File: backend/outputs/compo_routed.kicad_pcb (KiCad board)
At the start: 4 copper layers, 56 x 55 mm, 20 parts, among them J1 Conn_01x06_Pin, J2 Barrel_Jack, J3 Conn_01x02_Pin, U2 MIC5504-1.2YM5, U3 ATmega164P-20P

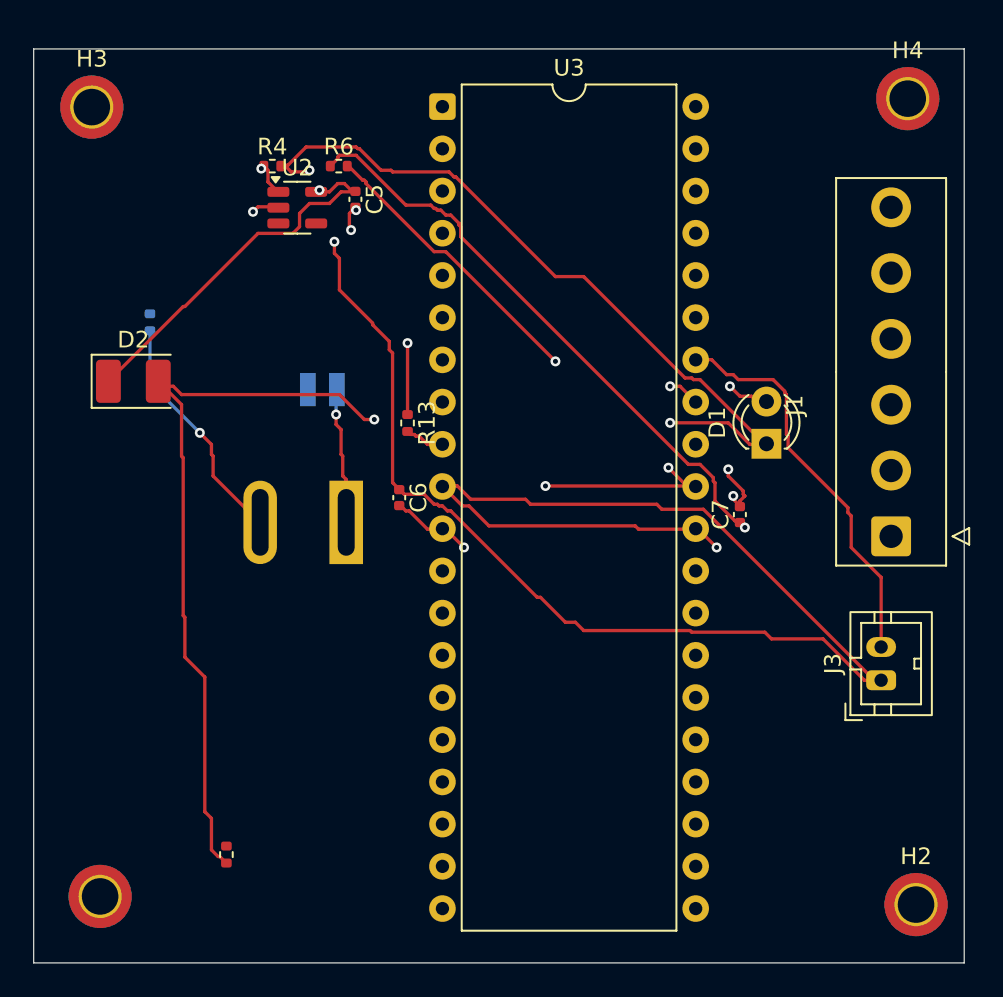
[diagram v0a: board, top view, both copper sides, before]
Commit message: Integrated Gemini 2.0 and added routing dashboard
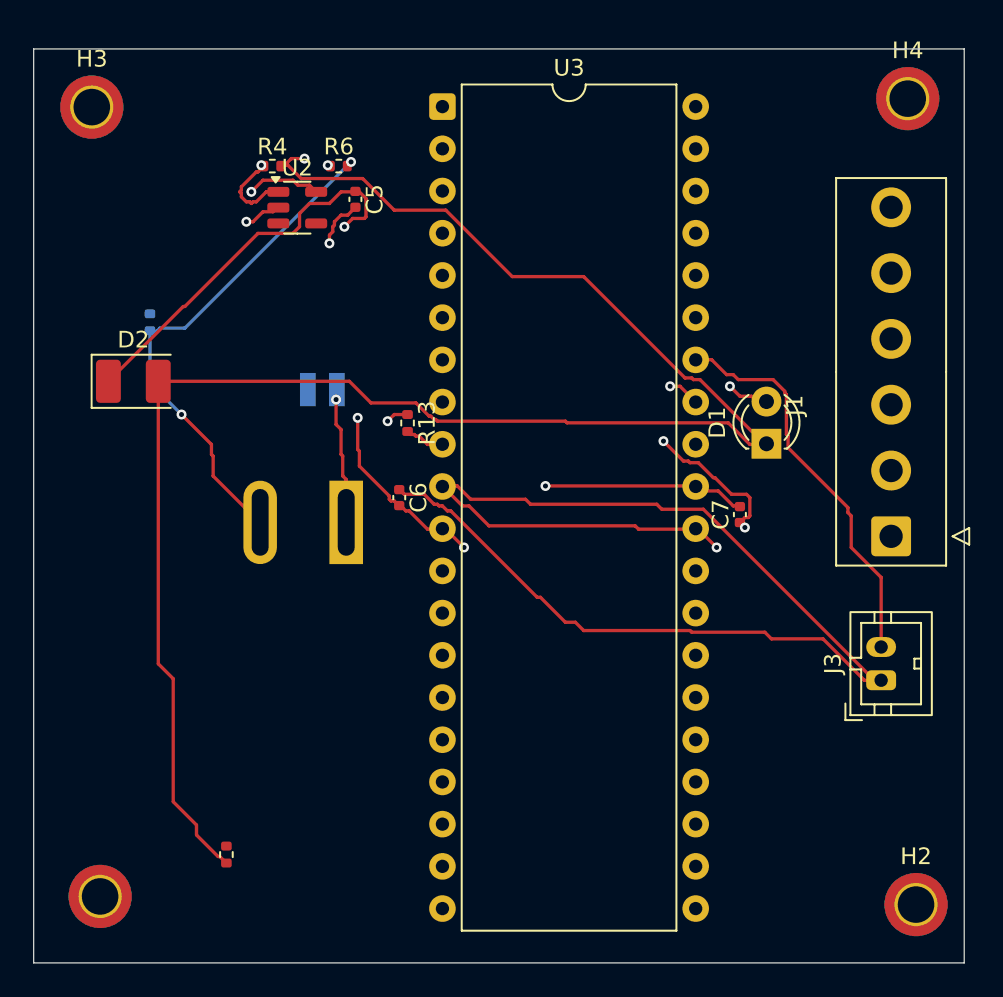
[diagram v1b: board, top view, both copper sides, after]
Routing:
- net +1V2: track 164.0 -> 155.8 mm, vias 4 -> 6
- net +3V3: track 20.6 -> 25.3 mm
- net GND: track 197.1 -> 193.4 mm, vias 13 -> 8

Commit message: Added SQLite history tracking and expanded design rule UI
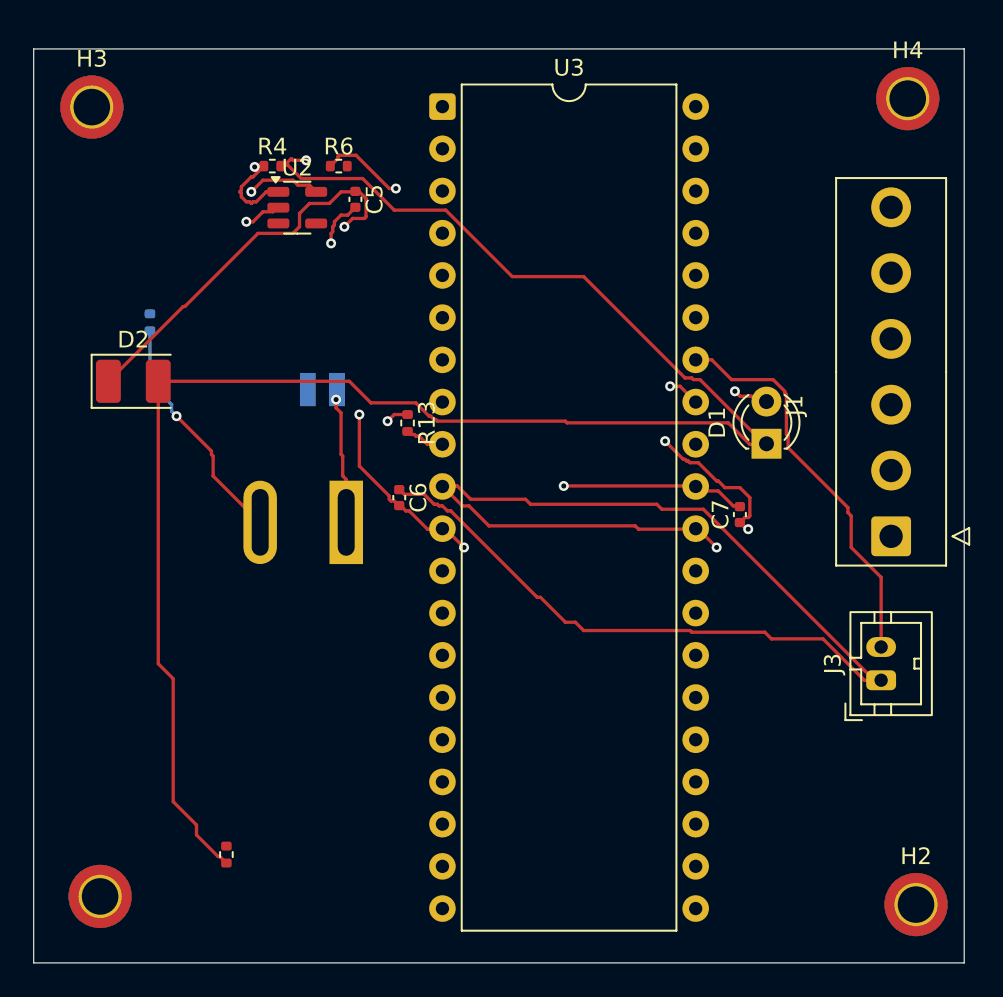
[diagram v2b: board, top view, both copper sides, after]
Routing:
- net GND: track 193.4 -> 176.7 mm, vias 8 -> 7
- net +1V2: track 155.8 -> 156.9 mm
- net +3V3: track 25.3 -> 25.8 mm
